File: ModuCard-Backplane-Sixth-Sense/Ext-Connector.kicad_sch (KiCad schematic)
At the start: 1 part, among them J2 09031967921

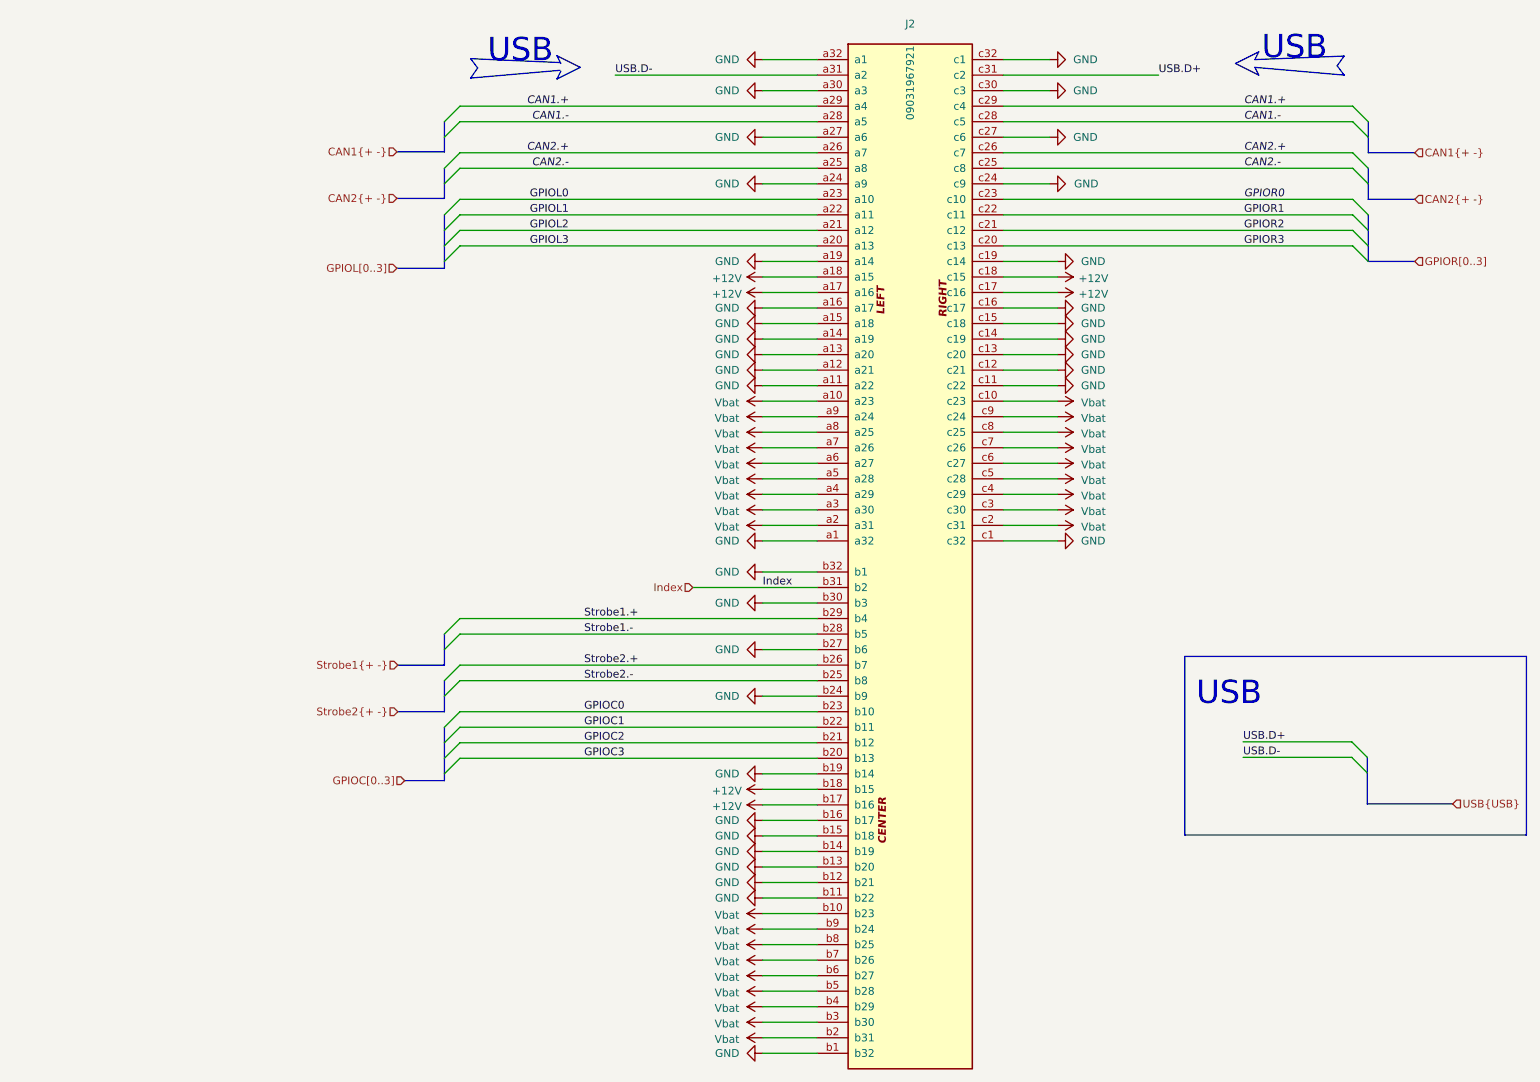
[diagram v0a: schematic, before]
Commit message: fix DRC errors, change pinout
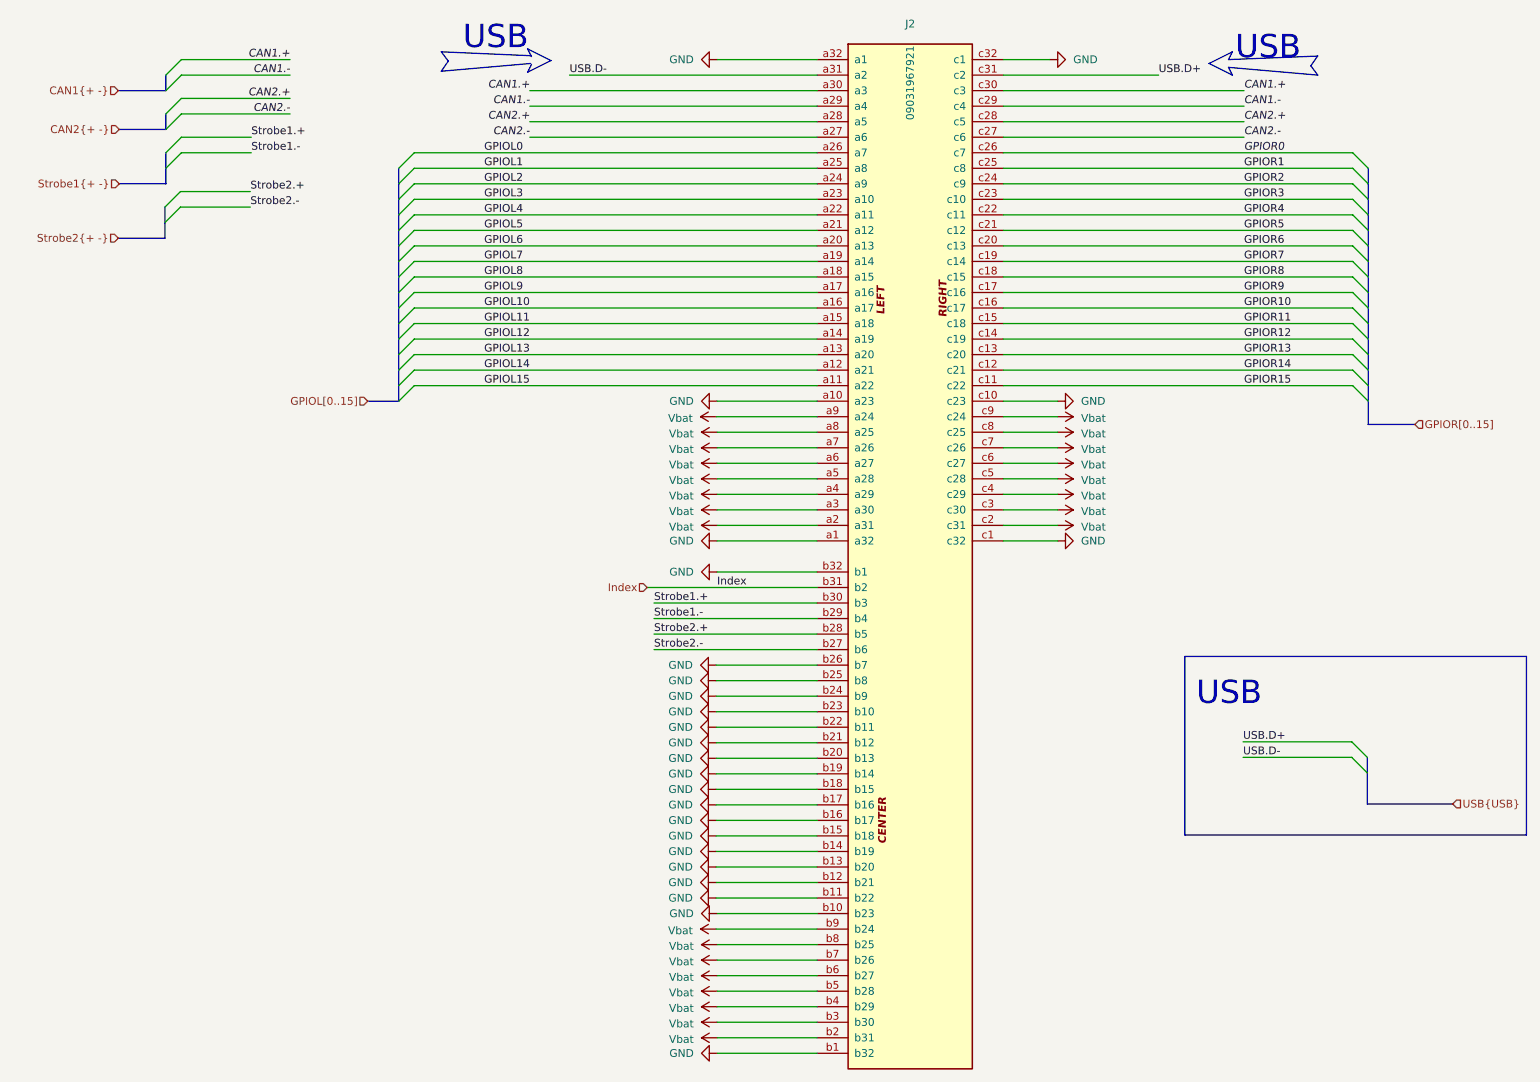
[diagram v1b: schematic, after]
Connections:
- net GPIOC0 is gone; now on net GND: J2.b23 (b10)
- net GPIOC1 is gone; now on net GND: J2.b22 (b11)
- net GPIOC2 is gone; now on net GND: J2.b21 (b12)
- net GPIOC3 is gone; now on net GND: J2.b20 (b13)
- net CAN1.+: now also J2.a30 (a3), J2.c30 (c3); no longer J2.a29 (a4), J2.c29 (c4)
- net CAN1.-: now also J2.a29 (a4), J2.c29 (c4); no longer J2.a28 (a5), J2.c28 (c5)
- net CAN2.+: now also J2.a28 (a5), J2.c28 (c5); no longer J2.a26 (a7), J2.c26 (c7)
- net CAN2.-: now also J2.a27 (a6), J2.c27 (c6); no longer J2.a25 (a8), J2.c25 (c8)
- net GND: now also J2.a10 (a23), J2.b10 (b23), J2.b17 (b16), J2.b18 (b15), J2.b25 (b8), J2.b26 (b7), J2.c10 (c23); no longer J2.a11 (a22), J2.a12 (a21), J2.a13 (a20), J2.a14 (a19), J2.a15 (a18), J2.a16 (a17), J2.a19 (a14), J2.a24 (a9), J2.a27 (a6), J2.a30 (a3), J2.b27 (b6), J2.b30 (b3), J2.c11 (c22), J2.c12 (c21), J2.c13 (c20), J2.c14 (c19), J2.c15 (c18), J2.c16 (c17), J2.c19 (c14), J2.c24 (c9), J2.c27 (c6), J2.c30 (c3)
- net GPIOL0: now also J2.a26 (a7); no longer J2.a23 (a10)
- net GPIOL1: now also J2.a25 (a8); no longer J2.a22 (a11)
- net GPIOL2: now also J2.a24 (a9); no longer J2.a21 (a12)
- net GPIOL3: now also J2.a23 (a10); no longer J2.a20 (a13)
- net GPIOR0: now also J2.c26 (c7); no longer J2.c23 (c10)
- net GPIOR1: now also J2.c25 (c8); no longer J2.c22 (c11)
- net GPIOR2: now also J2.c24 (c9); no longer J2.c21 (c12)
- net GPIOR3: now also J2.c23 (c10); no longer J2.c20 (c13)
- net Strobe1.+: now also J2.b30 (b3); no longer J2.b29 (b4)
- net Strobe1.-: now also J2.b29 (b4); no longer J2.b28 (b5)
- net Strobe2.+: now also J2.b28 (b5); no longer J2.b26 (b7)
- net Strobe2.-: now also J2.b27 (b6); no longer J2.b25 (b8)
- net Vbat: no longer J2.a10 (a23), J2.b10 (b23), J2.c10 (c23)
- removed net +12V: J2.a17 (a16), J2.a18 (a15), J2.b17 (b16), J2.b18 (b15), J2.c17 (c16), J2.c18 (c15)
- new net GPIOL10: J2.a16 (a17)
- new net GPIOL11: J2.a15 (a18)
- new net GPIOL12: J2.a14 (a19)
- new net GPIOL13: J2.a13 (a20)
- new net GPIOL14: J2.a12 (a21)
- new net GPIOL15: J2.a11 (a22)
- new net GPIOL4: J2.a22 (a11)
- new net GPIOL5: J2.a21 (a12)
- new net GPIOL6: J2.a20 (a13)
- new net GPIOL7: J2.a19 (a14)
- new net GPIOL8: J2.a18 (a15)
- new net GPIOL9: J2.a17 (a16)
- new net GPIOR10: J2.c16 (c17)
- new net GPIOR11: J2.c15 (c18)
- new net GPIOR12: J2.c14 (c19)
- new net GPIOR13: J2.c13 (c20)
- new net GPIOR14: J2.c12 (c21)
- new net GPIOR15: J2.c11 (c22)
- new net GPIOR4: J2.c22 (c11)
- new net GPIOR5: J2.c21 (c12)
- new net GPIOR6: J2.c20 (c13)
- new net GPIOR7: J2.c19 (c14)
- new net GPIOR8: J2.c18 (c15)
- new net GPIOR9: J2.c17 (c16)

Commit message: project overhaul
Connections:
- net GND: no longer J2.b32 (b1)
- net Index renamed Index2
- new net Index1: J2.b32 (b1)
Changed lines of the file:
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@@
 	)
 	(bus_entry
-		(at 35.7124 33.02)
+		(at 66.1924 140.97)
 		(size -2.54 2.54)
 		(stroke
@@
 	)
 	(bus_entry
-		(at 35.7124 26.67)
+		(at 66.1924 134.62)
 		(size -2.54 2.54)
 		(stroke
@@
 	)
 	(bus_entry
-		(at 35.7124 35.56)
+		(at 66.1924 143.51)
 		(size -2.54 2.54)
 		(stroke
@@
 	)
 	(bus_entry
-		(at 33.1724 44.45)
+		(at 63.6524 152.4)
 		(size 2.54 -2.54)
 		(stroke
@@
 	)
 	(bus_entry
-		(at 33.1724 41.91)
+		(at 63.6524 149.86)
 		(size 2.54 -2.54)
 		(stroke
@@
 	)
 	(bus_entry
-		(at 33.02 50.8)
+		(at 63.5 158.75)
 		(size 2.54 -2.54)
 		(stroke
@@
 	)
 	(bus_entry
-		(at 33.02 53.34)
+		(at 63.5 161.29)
 		(size 2.54 -2.54)
 		(stroke
@@
 	)
 	(bus_entry
-		(at 35.7124 29.21)
+		(at 66.1924 137.16)
 		(size -2.54 2.54)
 		(stroke
@@
 	(wire
 		(pts
+			(xy 111.76 110.49) (xy 139.7 110.49)
+		)
+		(stroke
+			(width 0)
+			(type default)
+		)
+	)
+	(wire
+		(pts
 			(xy 123.3424 82.55) (xy 139.7 82.55)
 		)
@@
 	(wire
 		(pts
-			(xy 35.7124 26.67) (xy 53.4924 26.67)
+			(xy 66.1924 134.62) (xy 83.9724 134.62)
 		)
 		(stroke
@@
 	(wire
 		(pts
-			(xy 53.4924 35.56) (xy 35.7124 35.56)
+			(xy 83.9724 143.51) (xy 66.1924 143.51)
 		)
 		(stroke
@@
 	(wire
 		(pts
-			(xy 35.7124 39.37) (xy 47.1424 39.37)
+			(xy 66.1924 147.32) (xy 77.6224 147.32)
 		)
 		(stroke
@@
 	(bus
 		(pts
-			(xy 33.1724 44.45) (xy 33.1724 46.99)
+			(xy 63.6524 152.4) (xy 63.6524 154.94)
 		)
 		(stroke
@@
 	(wire
 		(pts
-			(xy 123.3424 110.49) (xy 139.7 110.49)
-		)
-		(stroke
-			(width 0)
-			(type default)
-		)
-	)
-	(wire
-		(pts
-			(xy 35.7124 29.21) (xy 53.4924 29.21)
+			(xy 66.1924 137.16) (xy 83.9724 137.16)
 		)
 		(stroke
@@
 	(wire
 		(pts
-			(xy 35.7124 41.91) (xy 47.1424 41.91)
+			(xy 66.1924 149.86) (xy 77.6224 149.86)
 		)
 		(stroke
@@
 	(bus
 		(pts
-			(xy 33.1724 41.91) (xy 33.1724 44.45)
+			(xy 63.6524 149.86) (xy 63.6524 152.4)
 		)
 		(stroke
@@
 	(bus
 		(pts
-			(xy 25.4 55.88) (xy 33.02 55.88)
+			(xy 55.88 163.83) (xy 63.5 163.83)
 		)
 		(stroke
@@
 	(wire
 		(pts
+			(xy 111.9124 113.03) (xy 139.7 113.03)
+		)
+		(stroke
+			(width 0)
+			(type default)
+		)
+	)
+	(wire
+		(pts
 			(xy 179.07 100.33) (xy 170.18 100.33)
 		)
@@
 	(wire
 		(pts
-			(xy 35.56 48.26) (xy 46.99 48.26)
+			(xy 66.04 156.21) (xy 77.47 156.21)
 		)
 		(stroke
@@
 	(wire
 		(pts
-			(xy 53.4924 33.02) (xy 35.7124 33.02)
+			(xy 83.9724 140.97) (xy 66.1924 140.97)
 		)
 		(stroke
@@
 	(bus
 		(pts
-			(xy 33.02 50.8) (xy 33.02 53.34)
+			(xy 63.5 158.75) (xy 63.5 161.29)
 		)
 		(stroke
@@
 	(bus
 		(pts
-			(xy 25.5524 31.75) (xy 33.1724 31.75)
+			(xy 56.0324 139.7) (xy 63.6524 139.7)
 		)
 		(stroke
@@
 	(bus
 		(pts
-			(xy 33.02 53.34) (xy 33.02 55.88)
+			(xy 63.5 161.29) (xy 63.5 163.83)
 		)
 		(stroke
@@
 	(bus
 		(pts
-			(xy 25.5524 46.99) (xy 33.1724 46.99)
+			(xy 56.0324 154.94) (xy 63.6524 154.94)
 		)
 		(stroke
@@
 	(wire
 		(pts
-			(xy 111.9124 113.03) (xy 139.7 113.03)
-		)
-		(stroke
-			(width 0)
-			(type default)
-		)
-	)
-	(wire
-		(pts
 			(xy 123.3424 97.79) (xy 139.7 97.79)
 		)
@@
 	(wire
 		(pts
-			(xy 35.56 50.8) (xy 46.99 50.8)
+			(xy 66.04 158.75) (xy 77.47 158.75)
 		)
 		(stroke
@@
 	(bus
 		(pts
-			(xy 25.5524 38.1) (xy 33.1724 38.1)
+			(xy 56.0324 146.05) (xy 63.6524 146.05)
 		)
 		(stroke
@@
 	(bus
 		(pts
-			(xy 33.1724 35.56) (xy 33.1724 38.1)
+			(xy 63.6524 143.51) (xy 63.6524 146.05)
 		)
 		(stroke
@@
 	(bus
 		(pts
-			(xy 33.1724 29.21) (xy 33.1724 31.75)
+			(xy 63.6524 137.16) (xy 63.6524 139.7)
 		)
 		(stroke
@@
 	)
 	(label "Strobe2.-"
-		(at 46.99 50.8 0)
+		(at 77.47 158.75 0)
 		(effects
 			(font
@@
 	)
 	(label "CAN2.-"
-		(at 53.4924 35.56 180)
+		(at 83.9724 143.51 180)
 		(effects
 			(font
@@
 		)
 	)
-	(label "Index"
-		(at 123.3424 113.03 0)
-		(effects
-			(font
-				(size 1.27 1.27)
-			)
-			(justify left bottom)
-		)
-	)
 	(label "Strobe1.-"
-		(at 47.1424 41.91 0)
+		(at 77.6224 149.86 0)
 		(effects
 			(font
@@
 		)
 	)
+	(label "Index1"
+		(at 112.8776 110.49 0)
+		(effects
+			(font
+				(size 1.27 1.27)
+			)
+			(justify left bottom)
+		)
+	)
 	(label "CAN2.+"
 		(at 92.71 36.83 180)
@@
 	)
 	(label "Strobe1.+"
-		(at 47.1424 39.37 0)
+		(at 77.6224 147.32 0)
 		(effects
 			(font
@@
 		)
 	)
+	(label "Index2"
+		(at 113.03 113.03 0)
+		(effects
+			(font
+				(size 1.27 1.27)
+			)
+			(justify left bottom)
+		)
+	)
 	(label "USB.D-"
 		(at 209.3976 140.8176 0)
@@
 	)
 	(label "CAN2.+"
-		(at 53.4924 33.02 180)
+		(at 83.9724 140.97 180)
 		(effects
 			(font
@@
 	)
 	(label "CAN1.-"
-		(at 53.4924 29.21 180)
+		(at 83.9724 137.16 180)
 		(effects
 			(font
@@
 	)
 	(label "CAN1.+"
-		(at 53.4924 26.67 180)
+		(at 83.9724 134.62 180)
 		(effects
 			(font
@@
 	)
 	(label "Strobe2.+"
-		(at 46.99 48.26 0)
+		(at 77.47 156.21 0)
 		(effects
 			(font
@@
 		)
 	)
-	(hierarchical_label "Index"
+	(hierarchical_label "Strobe1{+ -}"
 		(shape input)
-		(at 111.9124 113.03 180)
+		(at 56.0324 154.94 180)
 		(effects
 			(font
@@
 		)
 	)
-	(hierarchical_label "Strobe1{+ -}"
-		(shape input)
-		(at 25.5524 46.99 180)
+	(hierarchical_label "Index2"
+		(shape bidirectional)
+		(at 111.9124 113.03 180)
 		(effects
 			(font
@@
 	(hierarchical_label "CAN2{+ -}"
 		(shape input)
-		(at 25.5524 38.1 180)
+		(at 56.0324 146.05 180)
 		(effects
 			(font
@@
 	(hierarchical_label "Strobe2{+ -}"
 		(shape input)
-		(at 25.4 55.88 180)
+		(at 55.88 163.83 180)
 		(effects
 			(font
@@
 	(hierarchical_label "CAN1{+ -}"
 		(shape input)
-		(at 25.4 31.75 180)
+		(at 55.88 139.7 180)
 		(effects
 			(font
@@
 		)
 	)
+	(hierarchical_label "Index1"
+		(shape bidirectional)
+		(at 111.76 110.49 180)
+		(effects
+			(font
+				(size 1.27 1.27)
+			)
+			(justify right)
+		)
+	)
 	(symbol
 		(lib_id "power:+12V")
@@
 					(unit 1)
 				)
-			)
-		)
-	)
-	(symbol
-		(lib_id "power:GND")
-		(at 123.3424 110.49 270)
-		(unit 1)
-		(body_style 1)
-		(exclude_from_sim no)
-		(in_bom yes)
-		(on_board yes)
-		(in_pos_files yes)
-		(dnp no)
-		(fields_autoplaced yes)
-		(property "Reference" "#PWR0206"
-			(at 116.9924 110.49 0)
-			(hide yes)
-			(show_name no)
-			(do_not_autoplace no)
-			(effects
-				(font
-					(size 1.27 1.27)
-				)
-			)
-		)
-		(property "Value" "GND"
-			(at 119.5324 110.4899 90)
-			(show_name no)
-			(do_not_autoplace no)
-			(effects
-				(font
-					(size 1.27 1.27)
-				)
-				(justify right)
-			)
-		)
-		(property "Footprint" ""
-			(at 123.3424 110.49 0)
-			(hide yes)
-			(show_name no)
-			(do_not_autoplace no)
-			(effects
-				(font
-					(size 1.27 1.27)
-				)
-			)
-		)
-		(property "Datasheet" ""
-			(at 123.3424 110.49 0)
-			(hide yes)
-			(show_name no)
-			(do_not_autoplace no)
-			(effects
-				(font
-					(size 1.27 1.27)
-				)
-			)
-		)
-		(property "Description" "Power symbol creates a global label with name \"GND\" , ground"
-			(at 123.3424 110.49 0)
-			(hide yes)
-			(show_name no)
-			(do_not_autoplace no)
-			(effects
-				(font
-					(size 1.27 1.27)
-				)
-			)
-		)
-		(pin "1"
-		)
-		(instances
-			(project "ModuCard-Backplane-Sixth-Sense"
-				(path "/b8e6d233-63ab-459d-a617-f62d9ba23c71/9c3b7bf6-9b3b-4209-b6b4-4854f1ffc4bb"
-					(reference "#PWR0206")
-					(unit 1)
-				)
